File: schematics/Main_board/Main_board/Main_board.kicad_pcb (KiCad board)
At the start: 4 copper layers, 48.3 x 78.7 mm, 31 parts, among them J1 USB_B_Micro, J2 Conn_01x16_Female, J3 TOUCH, Q1 UMH3N, U1 ESP32-S3-WROOM-1, U2 AP2112K-3.3, U3 BQ21040DBVR, U4 CH340G, U5 PCF8563T, U6 LCD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

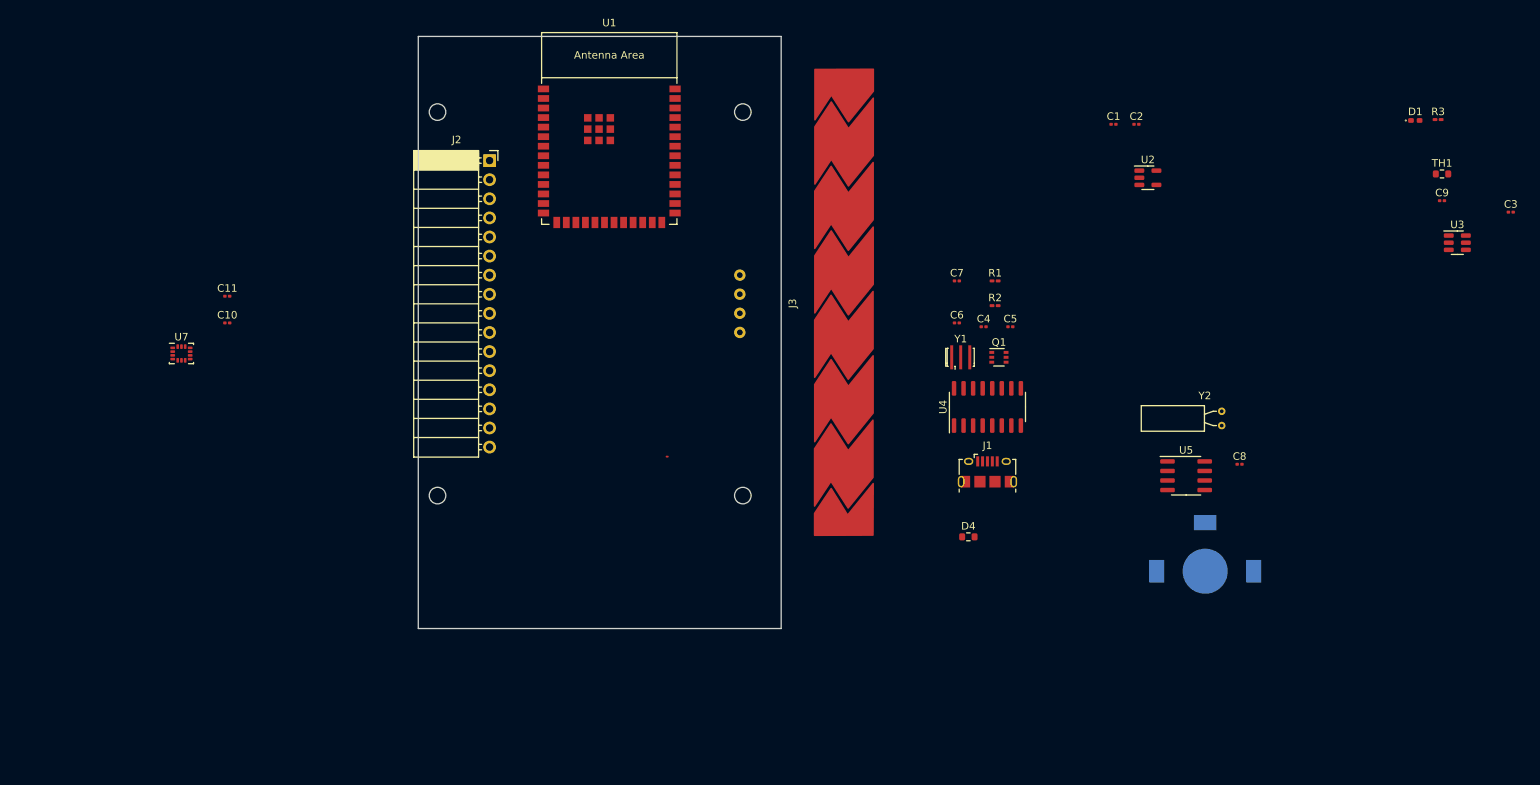
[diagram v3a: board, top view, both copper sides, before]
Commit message: Update: added datasheet to KiCad component
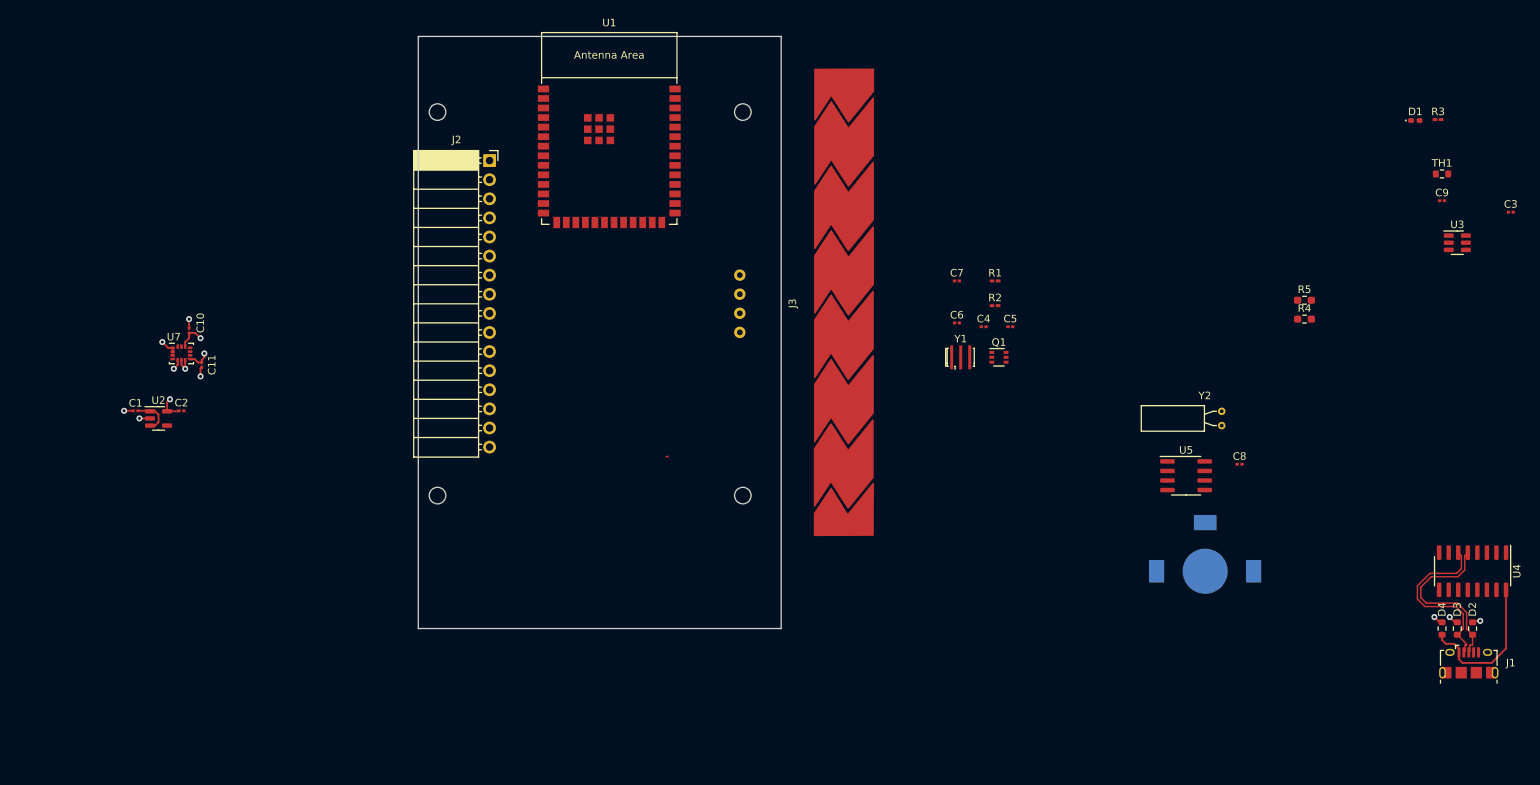
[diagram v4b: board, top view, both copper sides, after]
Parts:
- added D2: 0603ESDA-05N, Resistor_SMD:R_0603_1608Metric, F.Cu at (241.8, 116.8)
- added D3: 0603ESDA-05N, Resistor_SMD:R_0603_1608Metric, F.Cu at (239.8, 116.8)
- added R4: 4k7, Resistor_SMD:R_0603_1608Metric_Pad0.98x0.95mm_HandSolder, F.Cu at (219.5, 75.7)
- added R5: 4k7, Resistor_SMD:R_0603_1608Metric_Pad0.98x0.95mm_HandSolder, F.Cu at (219.5, 73.2)
- D4: value TPD1E10B06DPYR -> 0603ESDA-05N
- moved C1 135.5 mm to (64.0, 87.9), turned to 180 degrees
- moved U2 135.4 mm to (67.1, 88.9)
- moved C2 132.6 mm to (70.1, 87.9)
- moved J1 68.9 mm to (241.3, 121.4)
- moved U4 68.1 mm to (241.8, 109.2), turned to -90 degrees
- moved D4 64.2 mm to (237.7, 116.8), turned to 90 degrees
- moved C11 9.75 mm to (72.8, 81.8), turned to 90 degrees
- moved C10 5.18 mm to (71.1, 77.2), turned to 90 degrees
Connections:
- C10 pad 1: Net-(C10-Pad1) -> +3V3
- C11 pad 2: Net-(C11-Pad2) -> +3V3
- J3 pad 1: unconnected-(J3-Pad1) -> /TOUCH_1
- J3 pad 2: unconnected-(J3-Pad2) -> /TOUCH_2
- J3 pad 3: unconnected-(J3-Pad3) -> /TOUCH_3
- J3 pad 4: unconnected-(J3-Pad4) -> /TOUCH_4
- J3 pad 5: unconnected-(J3-Pad5) -> /TOUCH_5
- U1 pad 1: Net-(U1-Pad1) -> GNDREF
- U1 pad 12: unconnected-(U1-Pad12) -> /TOUCH_3
- U1 pad 17: unconnected-(U1-Pad17) -> /TOUCH_4
- U1 pad 18: unconnected-(U1-Pad18) -> /TOUCH_5
- U1 pad 19: unconnected-(U1-Pad19) -> /MOSI
- U1 pad 2: unconnected-(U1-Pad2) -> /3v3_IN_ESP32
- U1 pad 20: unconnected-(U1-Pad20) -> /SPI_CLK
- U1 pad 21: unconnected-(U1-Pad21) -> /MISO
- U1 pad 22: unconnected-(U1-Pad22) -> /TOUCH_1
- U1 pad 40: Net-(U1-Pad1) -> GNDREF
- U1 pad 41: Net-(U1-Pad1) -> GNDREF
- U1 pad 6: unconnected-(U1-Pad6) -> /TOUCH_1
- U1 pad 7: unconnected-(U1-Pad7) -> /TOUCH_2
- U7 pad 1: unconnected-(U7-Pad1) -> GNDREF
- U7 pad 12: unconnected-(U7-Pad12) -> +3.3V
- U7 pad 4: unconnected-(U7-Pad4) -> /INT_1_MPU
- U7 pad 5: Net-(C10-Pad1) -> +3V3
- U7 pad 8: Net-(C11-Pad2) -> +3V3
- U7 pad 9: unconnected-(U7-Pad9) -> /INT_2_MPU
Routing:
- net /D-: track 0.00 -> 24.0 mm
- net /D+: track 0.00 -> 23.6 mm
- net +5V: track 0.00 -> 19.9 mm
- net GNDREF: track 0.00 -> 14.0 mm, vias 0 -> 9
- net +3V3: track 0.00 -> 11.6 mm, vias 0 -> 4
- net +BATT: track 0.00 -> 5.28 mm

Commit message: Update: First pcb revision complete
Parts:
- added BT2: 3v7 LIpo, LCD:lipo_battery_800mA, B.Cu at (138.7, 78.1)
- added H1: MountingHole, MountingHole:MountingHole_3.5mm_Pad_Via, F.Cu at (163.8, 49.8)
- added H2: MountingHole, MountingHole:MountingHole_3.5mm_Pad_Via, F.Cu at (114.2, 49.8)
- added H3: MountingHole, MountingHole:MountingHole_3.5mm_Pad_Via, F.Cu at (114.2, 109.9)
- added H4: MountingHole, MountingHole:MountingHole_3.5mm_Pad_Via, F.Cu at (163.8, 109.8)
- added H5: MountingHole, MountingHole:MountingHole_2.2mm_M2_DIN965, F.Cu at (164.3, 121.3)
- added H6: MountingHole, MountingHole:MountingHole_2.2mm_M2_DIN965, F.Cu at (112.6, 121.3)
- added H7: MountingHole, MountingHole:MountingHole_2.2mm_M2_DIN965, F.Cu at (112.8, 129.3)
- added H8: MountingHole, MountingHole:MountingHole_2.2mm_M2_DIN965, F.Cu at (164.3, 129.3)
- added J4: Conn_01x06_Female, LCD:slide_sensor_6p, F.Cu at (130.2, 125.3)
- added J5: Conn_01x06_Female, LCD:slider_sensors_points_smd, F.Cu at (138.7, 120.6)
- added R6: 1K, Resistor_SMD:R_0201_0603Metric_Pad0.64x0.40mm_HandSolder, F.Cu at (141.5, 91.2)
- C8: value 8p -> 22p
- J3: value TOUCH -> Conn_01x06_Female; footprint LCD:slide_sensor_8p -> LCD:slider_sensors_points_smd
- R3: value 120 -> 1k5
- TH1: moved to B.Cu
- U1: footprint esp:ESP32-S3-WROOM-2 -> esp:ESP32-S3-WROOM-1
- U3: value BQ21040DBVR -> bq21040; footprint Package_TO_SOT_SMD:SOT-23-6 -> Package_TO_SOT_SMD:SOT-23-6_Handsoldering
- U6: moved to F.Cu
- Y1: value 12Mhz -> Crystal_GND2_Small
- moved C3 111.5 mm to (139.4, 91.2), turned to -90 degrees
- moved D3 110.5 mm to (131.8, 93.2)
- moved D2 110.5 mm to (133.9, 93.2)
- moved D4 110.5 mm to (129.8, 93.2)
- moved U4 110.5 mm to (133.9, 85.6)
- moved J1 108.9 mm to (133.3, 106.8)
- moved R3 106.3 mm to (143.0, 98.3), turned to 180 degrees
- moved C9 104.3 mm to (140.8, 98.3), turned to 180 degrees
- moved U3 103.6 mm to (140.5, 95.1), turned to 90 degrees
- moved D1 101.3 mm to (145.5, 98.3), turned to 180 degrees
- moved TH1 100.7 mm to (138.9, 75.9), turned to 180 degrees
- moved U7 81.1 mm to (151.1, 82.5), turned to 180 degrees
- moved C10 79.4 mm to (150.1, 85.6), turned to -90 degrees
- moved C1 76.5 mm to (140.0, 79.0)
- moved C2 76.5 mm to (146.1, 79.0)
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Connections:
- C3 pad 1: Net-(C3-Pad1) -> GNDREF
- C3 pad 2: GNDREF -> +5V
- C9 pad 1: +3.3V -> GNDREF
- C9 pad 2: Net-(C9-Pad2) -> +BATT
- D1 pad 1: GNDREF -> Net-(D1-Pad1)
- J2 pad 10: /I/O_1 -> /SDA_1
- J2 pad 11: /I/O_2 -> /SCL_1
- J2 pad 12: /I/O_3 -> /MOSI
- J2 pad 13: /I/O_4 -> /MISO
- J2 pad 14: /I/O_5 -> /SPI_CLK
- J2 pad 3: /UART_TX -> /I/O_1
- J2 pad 4: /UART_RX -> /I/O_2
- J2 pad 5: /MOSI -> /I/O_3
- J2 pad 6: /MISO -> /I/O_4
- J2 pad 7: /SPI_CLK -> /I/O_5
- J2 pad 8: /SDA_1 -> /UART_TX
- J2 pad 9: /SCL_1 -> /UART_RX
- J3 pad 6: unconnected-(J3-Pad6) -> /TOUCH_6
- R3 pad 2: /NCH_CH_PIN -> +BATT
- U1 pad 22: /TOUCH_1 -> /TOUCH_6
- U3 pad 2: Net-(C9-Pad2) -> +BATT
- U3 pad 3: /NCH_CH_PIN -> Net-(D1-Pad1)
- U3 pad 4: unconnected-(U3-Pad4) -> Net-(R6-Pad1)
- U3 pad 5: Net-(C3-Pad1) -> GNDREF
- U3 pad 6: GNDREF -> +5V
- U7 pad 12: +3.3V -> +3V3
- Y1 pad 2: Net-(C5-Pad1) -> GNDREF
- Y1 pad 3: (no net) -> Net-(C5-Pad1)
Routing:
- net /SCL_1: track 0.00 -> 90.1 mm, vias 0 -> 3
- net /SDA_1: track 0.00 -> 87.8 mm, vias 0 -> 3
- net /EN: track 0.00 -> 37.3 mm, vias 0 -> 3
- net /I/O_2: track 0.00 -> 37.0 mm, vias 0 -> 1
- net /SPI_CLK: track 0.00 -> 36.8 mm, vias 0 -> 1
- net /I/O_1: track 0.00 -> 35.9 mm, vias 0 -> 1
- net Net-(BT1-Pad1): track 0.00 -> 34.9 mm, vias 0 -> 2
- net /UART_RX0_PGR: track 0.00 -> 33.4 mm, vias 0 -> 2
- net /MISO: track 0.00 -> 33.1 mm, vias 0 -> 1
- net +BATT: track 5.28 -> 38.1 mm, vias 0 -> 2
- net /UART_TX0_PGR: track 0.00 -> 32.2 mm, vias 0 -> 2
- net /MOSI: track 0.00 -> 29.4 mm, vias 0 -> 1
- net /TOUCH_1: track 0.00 -> 27.1 mm, vias 0 -> 2
- net Net-(TH1-Pad1): track 0.00 -> 26.9 mm, vias 0 -> 2
- net /TOUCH_2: track 0.00 -> 25.5 mm, vias 0 -> 2
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- added copper zone on In1.Cu, net +3V3
- added copper zone on In2.Cu, net +3V3
- added copper zone on B.Cu, net GNDREF
- added copper zone on F.Cu, net GNDREF
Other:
- board size 48.3 x 78.7 mm -> 59.9 x 88.1 mm

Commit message: fix: 3d step file paths
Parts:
- C1, C10, C11, C2, C3, C4, C5, C6, C7, C8, C9: footprint Capacitor_SMD:C_0201_0603Metric -> Capacitor_SMD:C_0402_1005Metric
- D2, D3, D4: footprint Resistor_SMD:R_0603_1608Metric -> Resistor_SMD:R_0402_1005Metric
- R1, R2: footprint Resistor_SMD:R_0201_0603Metric_Pad0.64x0.40mm_HandSolder -> Resistor_SMD:R_0402_1005Metric
- R3: value 1k5 -> 1K; footprint Resistor_SMD:R_0201_0603Metric_Pad0.64x0.40mm_HandSolder -> Resistor_SMD:R_0402_1005Metric
- R4, R5: footprint Resistor_SMD:R_0603_1608Metric_Pad0.98x0.95mm_HandSolder -> Resistor_SMD:R_0402_1005Metric
- R6: value 1K -> 1k5; footprint Resistor_SMD:R_0201_0603Metric_Pad0.64x0.40mm_HandSolder -> Resistor_SMD:R_0402_1005Metric
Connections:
- net /1hz_CLKOUT renamed /Peripherals/1hz_CLKOUT
- net /INT_1_MPU renamed /Peripherals/INT_1_MPU
- net /INT_2_MPU renamed /Peripherals/INT_2_MPU
- net /INT_ALARM renamed /Peripherals/INT_ALARM
- D1 pad 2: Net-(D1-Pad2) -> Net-(D1-A)
- D2 pad 1: /D+ -> /Connectors/D+
- D3 pad 1: /D- -> /Connectors/D-
- J1 pad 2: /D- -> /Connectors/D-
- J1 pad 3: /D+ -> /Connectors/D+
- J2 pad 10: /SDA_1 -> /Connectors/SDA_1
- J2 pad 11: /SCL_1 -> /Connectors/SCL_1
- J2 pad 12: /MOSI -> /Connectors/MOSI
- J2 pad 13: /MISO -> /Connectors/MISO
- J2 pad 14: /SPI_CLK -> /Connectors/SPI_CLK
- J2 pad 3: /I/O_1 -> /Connectors/I_O_1
- J2 pad 4: /I/O_2 -> /Connectors/I_O_2
- J2 pad 5: /I/O_3 -> /Connectors/I_O_3
- J2 pad 6: /I/O_4 -> /Connectors/I_O_4
- J2 pad 7: /I/O_5 -> /Connectors/I_O_5
- J2 pad 8: /UART_TX -> /Connectors/UART_TX
- J2 pad 9: /UART_RX -> /Connectors/UART_RX
- J3 pad 1: /TOUCH_1 -> /Peripherals/TOUCH_1
- J3 pad 2: /TOUCH_2 -> /Peripherals/TOUCH_2
- J3 pad 3: /TOUCH_3 -> /Peripherals/TOUCH_3
- J3 pad 4: /TOUCH_4 -> /Peripherals/TOUCH_4
- J3 pad 5: /TOUCH_5 -> /Peripherals/TOUCH_5
- J3 pad 6: /TOUCH_6 -> /Peripherals/TOUCH_6
- R3 pad 1: Net-(D1-Pad2) -> Net-(U3-ISET)
- R3 pad 2: +BATT -> GNDREF
- R4 pad 1: /SDA_1 -> /Peripherals/SDA_1
- R5 pad 2: /SCL_1 -> /Peripherals/SCL_1
- R6 pad 1: Net-(R6-Pad1) -> Net-(D1-A)
- R6 pad 2: GNDREF -> +BATT
- U3 pad 4: Net-(R6-Pad1) -> Net-(U3-ISET)
- U5 pad 5: /SDA_1 -> /Peripherals/SDA_1
- U5 pad 6: /SCL_1 -> /Peripherals/SCL_1
- U6 pad 1: /SDA_1 -> /Peripherals/SDA_1
- U6 pad 2: /SCL_1 -> /Peripherals/SCL_1
- U7 pad 13: /SCL_1 -> /Peripherals/SCL_1
- U7 pad 14: /SDA_1 -> /Peripherals/SDA_1
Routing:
- net GNDREF: track 31.1 -> 30.0 mm, vias 21 -> 20
- net +BATT: track 38.1 -> 39.3 mm, vias 2 -> 3

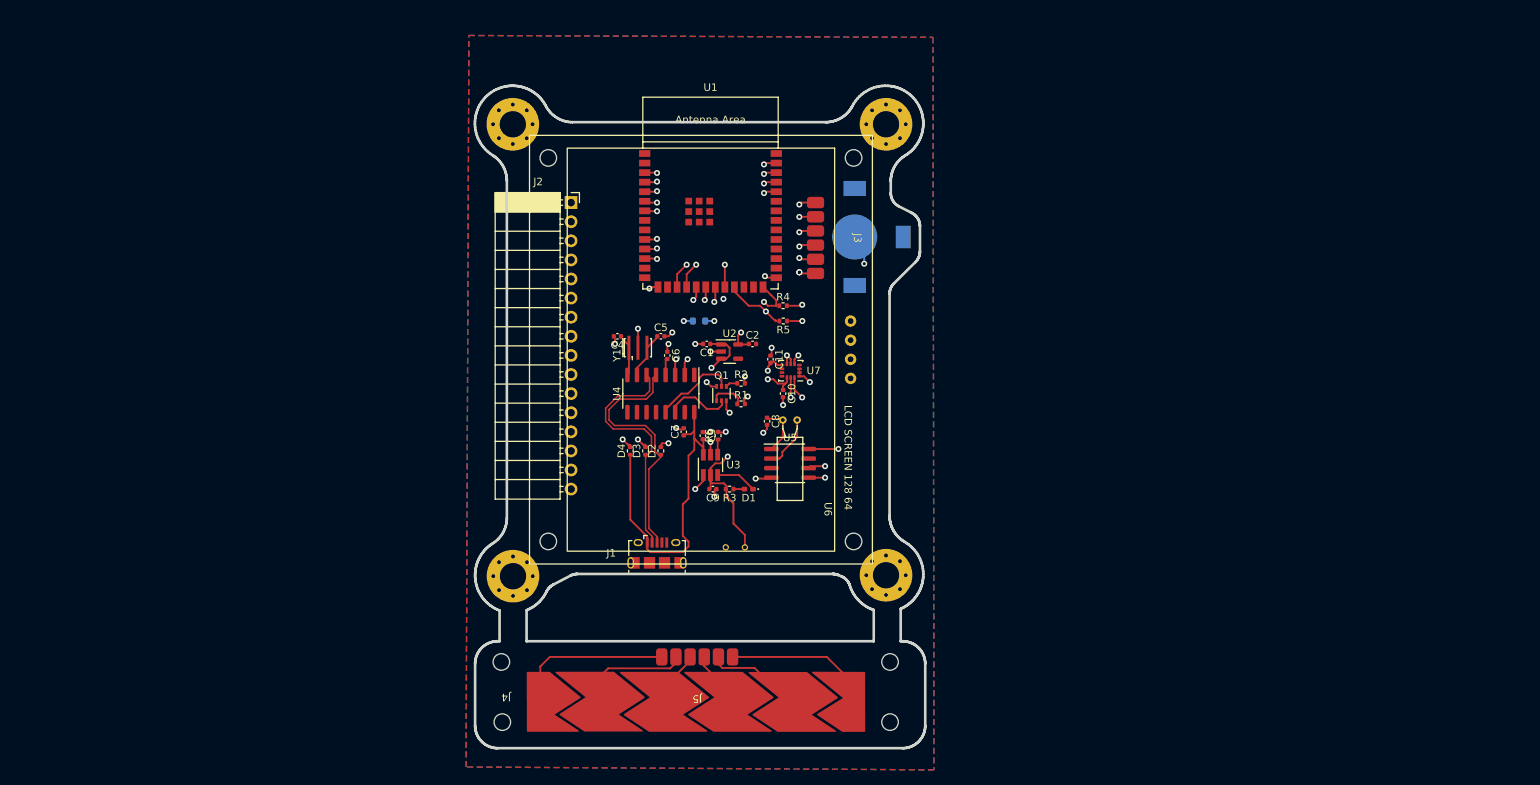
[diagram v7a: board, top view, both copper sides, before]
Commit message: update: All the resistors and capacitors footprints changed from 0603 to 0402
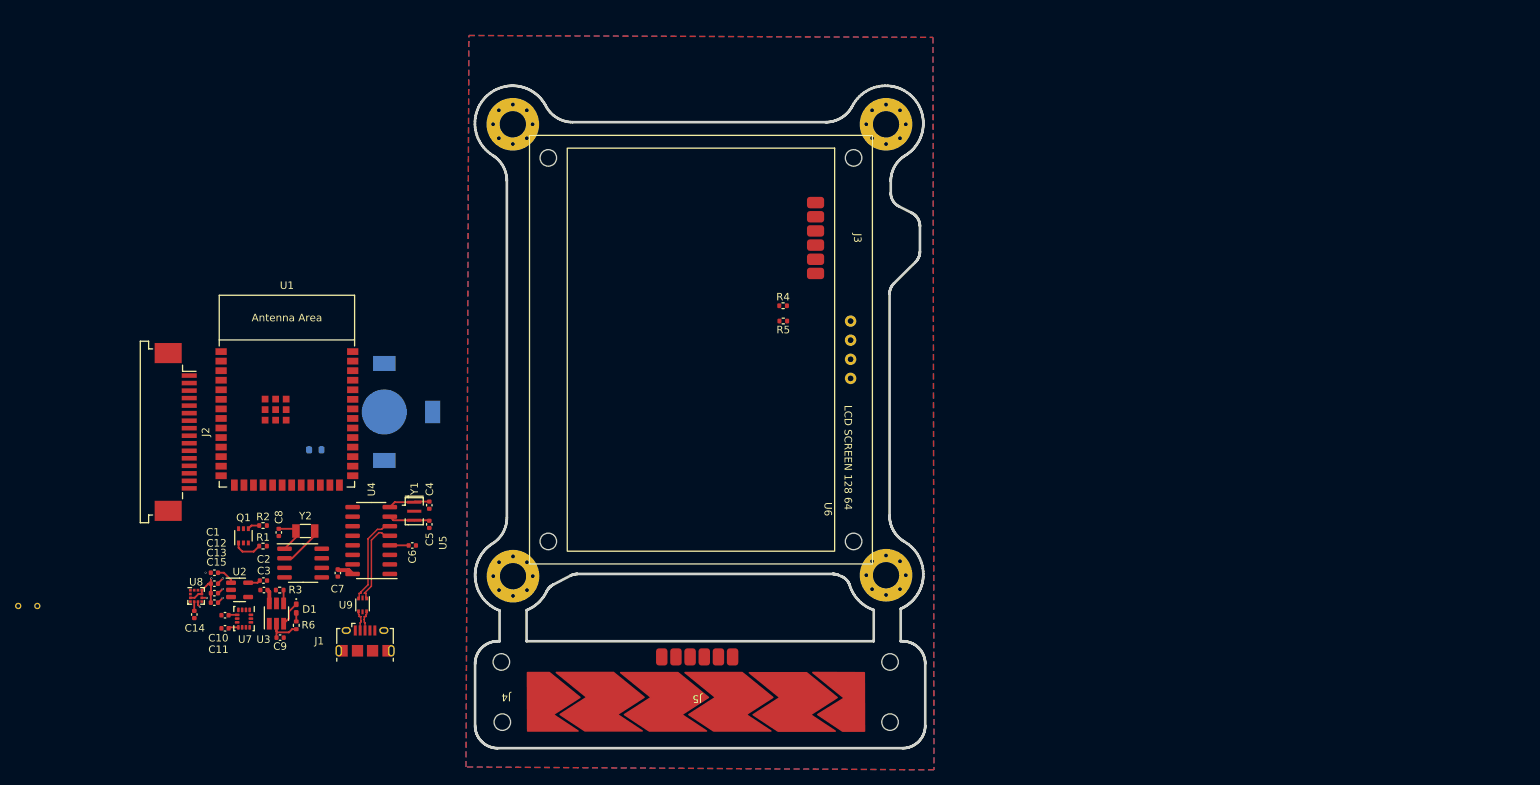
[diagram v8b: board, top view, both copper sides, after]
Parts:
- removed D2, D3, D4: 0603ESDA-05N, Resistor_SMD:R_0402_1005Metric
- added C12: 100nf, Capacitor_SMD:C_0402_1005Metric, F.Cu at (74.5, 110.9)
- added C13: 100nf, Capacitor_SMD:C_0402_1005Metric, F.Cu at (74.5, 112.1)
- added C14: 220nf, Capacitor_SMD:C_0402_1005Metric, F.Cu at (71.8, 115.0)
- added C15: 10uf, Capacitor_SMD:C_0402_1005Metric, F.Cu at (74.5, 113.4)
- added U8: LIS2MDL, Package_LGA:LGA-12_2x2mm_P0.5mm, F.Cu at (72.1, 112.5)
- added U9: USBLC6-2P6, Package_TO_SOT_SMD:SOT-666, F.Cu at (94.2, 113.7)
- J2: footprint Connector_PinSocket_2.54mm:PinSocket_1x16_P2.54mm_Horizontal -> Connector_FFC-FPC:TE_1-84953-6_1x16-1MP_P1.0mm_Horizontal
- Y1: footprint Crystal:Resonator_SMD_Murata_CSTxExxV-3Pin_3.0x1.1mm_HandSoldering -> Crystal:Resonator_SMD_Murata_CSTxExxV-3Pin_3.0x1.1mm
- Y2: footprint Crystal:Crystal_C38-LF_D3.0mm_L8.0mm_Horizontal -> Crystal:Crystal_SMD_3215-2Pin_3.2x1.5mm
- moved BT2 94.4 mm to (44.6, 85.9)
- moved C11 80.9 mm to (75.9, 116.8), turned to 0 degrees
- moved C10 79.9 mm to (75.9, 115.1), turned to 180 degrees
- moved U7 79.8 mm to (78.4, 115.5), turned to -90 degrees
- moved U2 72.5 mm to (77.8, 111.7)
- moved C2 72.3 mm to (81.0, 110.5)
- moved C1 72.2 mm to (74.5, 109.4)
- moved BT1 66.7 mm to (97.1, 88.0)
- moved C8 66.6 mm to (83.0, 104.1)
- moved R1 66.3 mm to (81.0, 105.9)
- moved R2 66.3 mm to (81.0, 103.1)
- moved Q1 66.3 mm to (78.3, 104.5)
- moved U5 66.1 mm to (86.3, 108.1)
- moved Y2 65.2 mm to (86.6, 103.9), turned to 180 degrees
- moved D1 62.2 mm to (85.4, 114.2), turned to -90 degrees
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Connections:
- J1 pad 1: +5V -> VBUS
- J1 pad 2: /Connectors/D- -> /Connectors/D_ESD-
- J1 pad 3: /Connectors/D+ -> /Connectors/D_ESD+
- J2 pad 10: /Connectors/SDA_1 -> /SDA_1
- J2 pad 11: /Connectors/SCL_1 -> /SCL_1
- J2 pad 12: /Connectors/MOSI -> /MOSI
- J2 pad 13: /Connectors/MISO -> /MISO
- J2 pad 14: /Connectors/SPI_CLK -> /SPI_CLK
- J2 pad 3: /Connectors/I_O_1 -> /I/O_1
- J2 pad 4: /Connectors/I_O_2 -> /I/O_2
- J2 pad 5: /Connectors/I_O_3 -> /I/O_3
- J2 pad 6: /Connectors/I_O_4 -> /I/O_4
- J2 pad 7: /Connectors/I_O_5 -> /I/O_5
- J2 pad 8: /Connectors/UART_TX -> /UART_TX0_PGR
- J2 pad 9: /Connectors/UART_RX -> /UART_RX0_PGR
- J3 pad 1: /Peripherals/TOUCH_1 -> /TOUCH_1
- J3 pad 2: /Peripherals/TOUCH_2 -> /TOUCH_2
- J3 pad 3: /Peripherals/TOUCH_3 -> /TOUCH_3
- J3 pad 4: /Peripherals/TOUCH_4 -> /TOUCH_4
- J3 pad 5: /Peripherals/TOUCH_5 -> /TOUCH_5
- J3 pad 6: /Peripherals/TOUCH_6 -> /TOUCH_6
- R4 pad 1: /Peripherals/SDA_1 -> /SCL_1
- R5 pad 2: /Peripherals/SCL_1 -> /SDA_1
- U5 pad 5: /Peripherals/SDA_1 -> /SCL_1
- U5 pad 6: /Peripherals/SCL_1 -> /SDA_1
- U6 pad 1: /Peripherals/SDA_1 -> /SCL_1
- U6 pad 2: /Peripherals/SCL_1 -> /SDA_1
- U7 pad 13: /Peripherals/SCL_1 -> /SDA_1
- U7 pad 14: /Peripherals/SDA_1 -> /SCL_1
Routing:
- net /SCL_1: track 90.1 -> 0.00 mm, vias 3 -> 0
- net /SDA_1: track 87.8 -> 0.00 mm, vias 3 -> 0
- net +5V: track 43.4 -> 4.09 mm
- net /EN: track 37.3 -> 0.00 mm, vias 3 -> 0
- net /I/O_2: track 37.0 -> 0.00 mm, vias 1 -> 0
- net /SPI_CLK: track 36.8 -> 0.00 mm, vias 1 -> 0
- net /I/O_1: track 35.9 -> 0.00 mm, vias 1 -> 0
- net Net-(BT1-+): track 34.9 -> 0.00 mm, vias 2 -> 0
- net /UART_RX0_PGR: track 33.4 -> 0.00 mm, vias 2 -> 0
- net /MISO: track 33.1 -> 0.00 mm, vias 1 -> 0
- net /UART_TX0_PGR: track 32.2 -> 0.00 mm, vias 2 -> 0
- net +BATT: track 39.3 -> 8.17 mm, vias 3 -> 0
- net /MOSI: track 29.4 -> 0.00 mm, vias 1 -> 0
- net /TOUCH_1: track 27.1 -> 0.00 mm, vias 2 -> 0
- net Net-(U3-TS): track 26.9 -> 0.00 mm, vias 2 -> 0
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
